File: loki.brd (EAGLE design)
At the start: 80 x 49 mm, 56 parts, among them IC2 LM358D, Q1 MOSFET-PCHANNELSMD, U1 USD SOCKET, X1 USBSMD, Y1 XRCGB_XTAL

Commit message: Minor layout changes; improvements to 2 pin plank template.
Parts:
- R3: device resistor:R0805 -> resistor:R0603
- moved F1 20.5 mm to (49.4, 14.0), turned to 0 degrees
- moved R2 14.6 mm to (56.1, 18.2)
- moved R1 13.6 mm to (54.0, 19.4), turned to 270 degrees
- moved R3 4.26 mm to (8.69, 35.9)
- moved C7 1.91 mm to (13.2, 35.8)
- moved R9 1.91 mm to (11.1, 35.8)
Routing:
- net USBVCC: track 43.0 -> 18.2 mm, vias 2 -> 0
- net D-: track 28.3 -> 6.26 mm
- net D+: track 26.3 -> 4.77 mm
- net N$15: track 3.51 -> 24.7 mm
- net N$4: track 4.16 -> 20.8 mm
- net N$2: track 2.39 -> 18.7 mm
- net N$20: track 68.3 -> 72.5 mm
- net N$25: track 6.85 -> 9.87 mm
- net +3V3: track 244.3 -> 246.5 mm
- net SDA0: track 42.3 -> 44.4 mm
- net SCL0: track 43.8 -> 45.6 mm
- net XRES: track 86.6 -> 88.0 mm
- net N$10: track 63.2 -> 63.9 mm

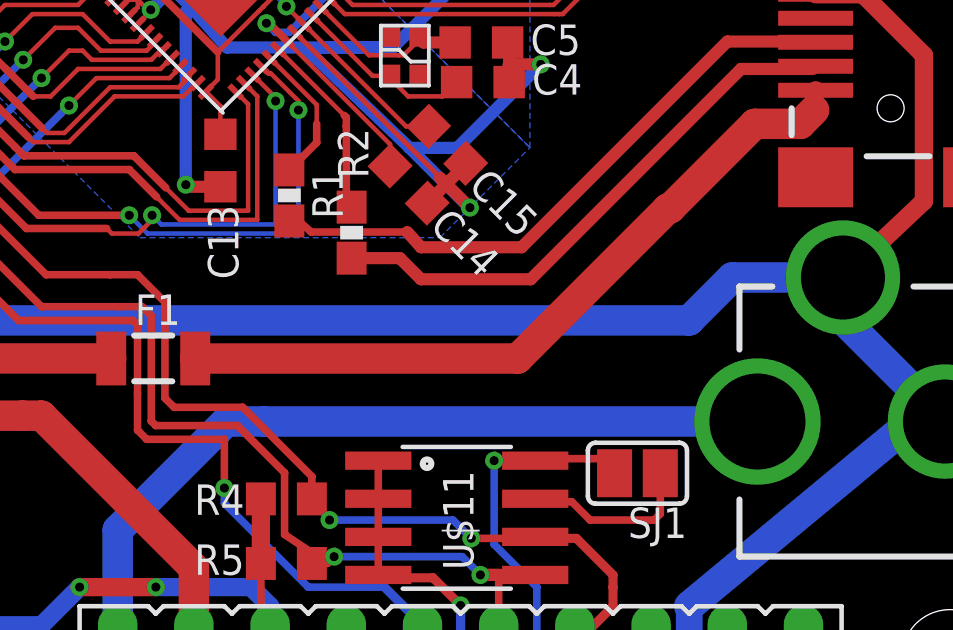
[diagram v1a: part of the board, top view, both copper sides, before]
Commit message: Added reverse polarity protection diode.
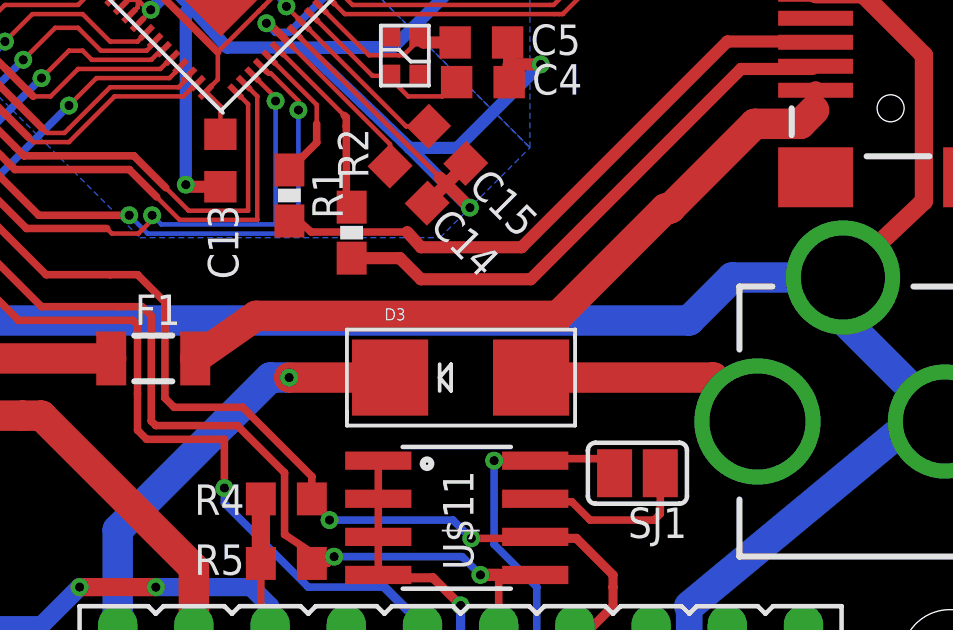
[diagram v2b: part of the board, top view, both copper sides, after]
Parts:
- added D3: (no value), adafruit:SMADIODE
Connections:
- new net N$11: CN1.PWR, D3.A
- net V+: now also D3.C; no longer CN1.PWR
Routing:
- net V+: track 80.5 -> 68.9 mm, vias 2 -> 3
- net N$11: track 0.00 -> 8.15 mm
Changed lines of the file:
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@@
 <element name="U$13" library="dp_devices" package="DP8049_V1" value="" x="0" y="0"/>
 <element name="U$6" library="loki" package="LOKI_LOGO" value="" x="39.7764" y="14.0208"/>
+<element name="D3" library="adafruit" package="SMADIODE" value="" x="59.69" y="13.335"/>
 </elements>
 <signals>
@@
 <contactref element="U$3" pad="P$5"/>
 <contactref element="R6" pad="1"/>
-<contactref element="CN1" pad="PWR"/>
 <wire x1="15.76" y1="9.72" x2="15.76" y2="8.705" width="0.6096" layer="1"/>
 <wire x1="15.76" y1="8.705" x2="15.445" y2="8.39" width="0.4064" layer="1"/>
@@
 <via x="29.21" y="4.1148" extent="1-16" drill="0.3"/>
 <wire x1="29.21" y1="4.1148" x2="28.575" y2="4.1148" width="0.254" layer="16"/>
-<wire x1="69.585" y1="11.87" x2="53.145" y2="11.87" width="1.016" layer="16"/>
-<wire x1="53.145" y1="11.87" x2="51.875" y2="11.87" width="1.016" layer="16"/>
 <wire x1="51.875" y1="11.87" x2="48.26" y2="8.255" width="1.016" layer="16"/>
 <wire x1="48.26" y1="8.255" x2="48.26" y2="4.445" width="1.016" layer="16"/>
 <wire x1="29.7898" y1="3.535" x2="47.35" y2="3.535" width="1.016" layer="1"/>
 <wire x1="47.35" y1="3.535" x2="48.26" y2="4.445" width="1.016" layer="1"/>
+<contactref element="D3" pad="C"/>
+<wire x1="57.3405" y1="13.335" x2="53.975" y2="13.335" width="1.016" layer="1"/>
+<via x="53.975" y="13.335" extent="1-16" drill="0.3"/>
+<wire x1="53.975" y1="13.335" x2="53.34" y2="13.335" width="1.016" layer="16"/>
+<wire x1="53.34" y1="13.335" x2="51.875" y2="11.87" width="1.016" layer="16"/>
 </signal>
 <signal name="N$6">
@@
 <wire x1="71.4756" y1="22.8632" x2="71.5236" y2="22.9112" width="0.6096" layer="1"/>
 <wire x1="66.6726" y1="18.9714" x2="66.5964" y2="18.9714" width="1.016" layer="1"/>
-<wire x1="66.5964" y1="18.9714" x2="61.595" y2="13.97" width="1.016" layer="1"/>
-<wire x1="61.595" y1="13.97" x2="50.8468" y2="13.97" width="1.016" layer="1"/>
 <wire x1="50.8468" y1="13.97" x2="50.8444" y2="13.9724" width="1.016" layer="1"/>
+<wire x1="66.5964" y1="18.9714" x2="66.5202" y2="18.9714" width="1.016" layer="1"/>
+<wire x1="66.5202" y1="18.9714" x2="62.9412" y2="15.3924" width="1.016" layer="1"/>
+<wire x1="62.9412" y1="15.3924" x2="52.874" y2="15.3924" width="1.016" layer="1"/>
+<wire x1="52.874" y1="15.3924" x2="50.8444" y2="13.9724" width="1.016" layer="1"/>
 </signal>
 <signal name="N$16">
@@
 <wire x1="8.5556" y1="34.925" x2="8.6882" y2="35.0576" width="0.254" layer="1"/>
 </signal>
+<signal name="N$11">
+<contactref element="CN1" pad="PWR"/>
+<contactref element="D3" pad="A"/>
+<wire x1="62.0395" y1="13.335" x2="68.12" y2="13.335" width="1.016" layer="1"/>
+<wire x1="68.12" y1="13.335" x2="69.585" y2="11.87" width="1.016" layer="1"/>
+</signal>
 </signals>

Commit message: Replace usb mini connector with usb micro one.
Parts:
- removed X1: USBSMD, SparkFun-Connectors:USB-MINIB
- added U$7: MICROUSB, ondraster:USB-MICROB
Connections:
- net GND: now also U$7.GND, U$7.SH1, U$7.SH2, U$7.SH3, U$7.SH4, U$7.SH5, U$7.SH6; no longer X1.GND
- net N$15: now also U$7.VBUS; no longer X1.VBUS
- net N$2: now also U$7.D-; no longer X1.D-
- net N$4: now also U$7.D+; no longer X1.D+
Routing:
- net GND: track 364.8 -> 377.8 mm
- net N$2: track 18.7 -> 23.2 mm
- net N$15: track 24.6 -> 29.1 mm
- net N$4: track 20.8 -> 25.2 mm
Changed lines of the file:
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@@
 <attribute name="NAME" x="55.6006" y="21.6455" size="1.016" layer="25" font="vector" rot="R270"/>
 </element>
-<element name="X1" library="SparkFun-Connectors" package="USB-MINIB" value="USBSMD" x="74.0236" y="24.5112" rot="R180"/>
 <element name="C3" library="resistor" package="C0603K" value="0.1u" x="47.1734" y="33.9336" smashed="yes" rot="R135">
 <attribute name="NAME" x="49.413065625" y="34.12749375" size="1.016" layer="25" rot="R135"/>
@@
 <element name="U$6" library="loki" package="LOKI_LOGO" value="" x="39.7764" y="14.0208"/>
 <element name="D3" library="adafruit" package="SMADIODE" value="" x="59.69" y="13.335"/>
+<element name="U$7" library="ondraster" package="USB-MICROB" value="MICROUSB" x="78.5622" y="24.5872" rot="R90"/>
 </elements>
 <signals>
@@
 <contactref element="U$2" pad="P$3"/>
 <contactref element="C17" pad="2"/>
-<contactref element="X1" pad="GND"/>
 <contactref element="U$3" pad="P$2"/>
 <contactref element="C19" pad="2"/>
@@
 <wire x1="55.88" y1="0.762" x2="21.803" y2="0.762" width="1.016" layer="16"/>
 <wire x1="21.803" y1="0.762" x2="20.525" y2="2.04" width="1.016" layer="16"/>
-<wire x1="71.5236" y1="26.1112" x2="73.1012" y2="26.1112" width="0.6096" layer="1"/>
-<wire x1="73.1012" y1="26.1112" x2="75.1332" y2="24.0792" width="0.6096" layer="1"/>
-<wire x1="75.1332" y1="24.0792" x2="75.1332" y2="19.2158" width="0.6096" layer="1"/>
 <wire x1="75.1332" y1="19.2158" x2="72.435" y2="16.67" width="0.6096" layer="1"/>
 <wire x1="29.1456" y1="46.5446" x2="26.035" y2="46.5446" width="0.6096" layer="1"/>
@@
 <contactref element="SV1" pad="2"/>
 <wire x1="55.88" y1="4.445" x2="55.88" y2="0.762" width="1.016" layer="16"/>
+<contactref element="U$7" pad="GND"/>
+<contactref element="U$7" pad="SH1"/>
+<contactref element="U$7" pad="SH6"/>
+<contactref element="U$7" pad="SH5"/>
+<contactref element="U$7" pad="SH4"/>
+<contactref element="U$7" pad="SH3"/>
+<contactref element="U$7" pad="SH2"/>
+<wire x1="75.9122" y1="25.8872" x2="76.9828" y2="25.8872" width="0.508" layer="1"/>
+<wire x1="76.9828" y1="25.8872" x2="77.47" y2="25.4" width="0.508" layer="1"/>
+<wire x1="77.47" y1="25.4" x2="77.47" y2="25.2984" width="0.508" layer="1"/>
+<wire x1="77.47" y1="25.2984" x2="77.47" y2="21.59" width="0.508" layer="1"/>
+<wire x1="77.47" y1="21.59" x2="77.47" y2="21.5526" width="0.508" layer="1"/>
+<wire x1="77.47" y1="21.5526" x2="75.1332" y2="19.2158" width="0.508" layer="1"/>
+<wire x1="75.8622" y1="27.0872" x2="77.5622" y2="27.0872" width="0.508" layer="1"/>
+<wire x1="77.5622" y1="27.0872" x2="78.5622" y2="28.0872" width="0.508" layer="1"/>
+<wire x1="78.5622" y1="25.5872" x2="78.5622" y2="24.5364" width="0.508" layer="1"/>
+<wire x1="78.5622" y1="24.5364" x2="78.5622" y2="23.5872" width="0.508" layer="1"/>
+<wire x1="77.47" y1="21.5526" x2="78.0968" y2="21.5526" width="0.508" layer="1"/>
+<wire x1="78.0968" y1="21.5526" x2="78.5622" y2="21.0872" width="0.508" layer="1"/>
+<wire x1="75.8622" y1="22.0872" x2="76.9728" y2="22.0872" width="0.508" layer="1"/>
+<wire x1="76.9728" y1="22.0872" x2="77.47" y2="21.59" width="0.508" layer="1"/>
+<wire x1="77.47" y1="25.4" x2="77.47" y2="25.2984" width="0.508" layer="1"/>
+<wire x1="77.47" y1="25.2984" x2="77.47" y2="24.638" width="0.508" layer="1"/>
+<wire x1="77.47" y1="24.638" x2="77.5716" y2="24.5364" width="0.508" layer="1"/>
+<wire x1="77.5716" y1="24.5364" x2="78.5622" y2="24.5364" width="0.508" layer="1"/>
+<wire x1="75.8622" y1="27.0872" x2="77.3068" y2="27.0872" width="0.508" layer="1"/>
+<wire x1="77.3068" y1="27.0872" x2="77.4192" y2="26.9748" width="0.508" layer="1"/>
+<wire x1="77.4192" y1="26.9748" x2="77.4192" y2="25.3492" width="0.508" layer="1"/>
+<wire x1="77.4192" y1="25.3492" x2="77.47" y2="25.2984" width="0.508" layer="1"/>
 </signal>
 <signal name="IND">
@@
 </signal>
 <signal name="N$2">
-<contactref element="X1" pad="D-"/>
 <contactref element="R2" pad="2"/>
 <wire x1="56.0578" y1="17.3157" x2="57.6651" y2="17.3157" width="0.4064" layer="1"/>
@@
 <wire x1="58.3692" y1="16.6116" x2="62.0268" y2="16.6116" width="0.4064" layer="1"/>
 <wire x1="62.0268" y1="16.6116" x2="69.0372" y2="23.622" width="0.4064" layer="1"/>
-<wire x1="69.0372" y1="23.622" x2="71.4344" y2="23.622" width="0.4064" layer="1"/>
-<wire x1="71.4344" y1="23.622" x2="71.5236" y2="23.7112" width="0.254" layer="1"/>
+<contactref element="U$7" pad="D-"/>
+<wire x1="75.9122" y1="23.9372" x2="69.3524" y2="23.9372" width="0.4064" layer="1"/>
+<wire x1="69.3524" y1="23.9372" x2="69.0372" y2="23.622" width="0.4064" layer="1"/>
 </signal>
 <signal name="N$4">
 <contactref element="R1" pad="2"/>
-<contactref element="X1" pad="D+"/>
 <wire x1="53.983" y1="18.5556" x2="54.2916" y2="18.5556" width="0.254" layer="1"/>
 <wire x1="54.2916" y1="18.5556" x2="54.7116" y2="18.1864" width="0.254" layer="1"/>
@@
 <wire x1="58.3692" y1="17.6784" x2="61.722" y2="17.6784" width="0.4064" layer="1"/>
 <wire x1="61.722" y1="17.6784" x2="68.58" y2="24.5364" width="0.4064" layer="1"/>
-<wire x1="68.58" y1="24.5364" x2="71.4984" y2="24.5364" width="0.4064" layer="1"/>
-<wire x1="71.4984" y1="24.5364" x2="71.5236" y2="24.5112" width="0.254" layer="1"/>
+<contactref element="U$7" pad="D+"/>
+<wire x1="75.9122" y1="24.5872" x2="68.6308" y2="24.5872" width="0.4064" layer="1"/>
+<wire x1="68.6308" y1="24.5872" x2="68.58" y2="24.5364" width="0.4064" layer="1"/>
 </signal>
 <signal name="D+">
@@
 </signal>
 <signal name="N$15">
-<contactref element="X1" pad="VBUS"/>
 <contactref element="F1" pad="2"/>
-<wire x1="66.6726" y1="18.9714" x2="69.4944" y2="21.7932" width="1.016" layer="1"/>
-<wire x1="69.4944" y1="21.7932" x2="71.0184" y2="21.7932" width="1.016" layer="1"/>
-<wire x1="71.0184" y1="21.7932" x2="71.4756" y2="22.2504" width="1.016" layer="1"/>
-<wire x1="71.4756" y1="22.2504" x2="71.4756" y2="22.8632" width="0.6096" layer="1"/>
-<wire x1="71.4756" y1="22.8632" x2="71.5236" y2="22.9112" width="0.6096" layer="1"/>
-<wire x1="66.6726" y1="18.9714" x2="66.5964" y2="18.9714" width="1.016" layer="1"/>
 <wire x1="50.8468" y1="13.97" x2="50.8444" y2="13.9724" width="1.016" layer="1"/>
-<wire x1="66.5964" y1="18.9714" x2="66.5202" y2="18.9714" width="1.016" layer="1"/>
-<wire x1="66.5202" y1="18.9714" x2="62.9412" y2="15.3924" width="1.016" layer="1"/>
+<wire x1="66.5202" y1="18.9714" x2="66.3194" y2="18.7706" width="1.016" layer="1"/>
+<wire x1="66.3194" y1="18.7706" x2="62.9412" y2="15.3924" width="1.016" layer="1"/>
 <wire x1="62.9412" y1="15.3924" x2="52.874" y2="15.3924" width="1.016" layer="1"/>
 <wire x1="52.874" y1="15.3924" x2="50.8444" y2="13.9724" width="1.016" layer="1"/>
+<contactref element="U$7" pad="VBUS"/>
+<wire x1="66.6726" y1="18.9714" x2="70.1778" y2="18.9714" width="1.016" layer="1"/>
+<wire x1="70.1778" y1="18.9714" x2="74.2188" y2="23.0124" width="1.016" layer="1"/>
+<wire x1="75.9122" y1="23.2872" x2="74.4936" y2="23.2872" width="0.508" layer="1"/>
+<wire x1="74.4936" y1="23.2872" x2="74.2188" y2="23.0124" width="0.508" layer="1"/>
+<wire x1="66.6726" y1="18.9714" x2="66.5202" y2="18.9714" width="0.508" layer="1"/>
+<wire x1="66.5202" y1="18.9714" x2="66.3194" y2="18.7706" width="0.508" layer="1"/>
 </signal>
 <signal name="N$16">

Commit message: Widened a few traces where possible.
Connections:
- net GND: no longer U$7.SH1, U$7.SH2, U$7.SH3, U$7.SH4, U$7.SH5, U$7.SH6
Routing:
- net GND: track 377.8 -> 364.1 mm
- net P3[0]: track 30.9 -> 32.2 mm
- net P3[1]: track 26.5 -> 27.6 mm
